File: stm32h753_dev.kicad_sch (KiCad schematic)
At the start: 88 parts, among them J1 Conn_02x38_Counter_Clockwise, J2 Conn_02x38_Counter_Clockwise, J3 USB_C_Receptacle_USB2.0_16P, J4 USB_C_Receptacle_USB2.0_16P, J5 DE9_Pins_MountingHoles, J6 Conn_01x05_Pin, J7 Conn_ARM_JTAG_SWD_10, SW1 SW_Push, SW2 SW_Push, U1 STM32H753IITx, U2 ST1S40IDR, U3 TPS2121RUX, U4 USB3300-EZK, U5 MCP2562-E-SN, U6 W25Q128JVS, Y1 SG-210STF, Y2 8MHz, Y3 Crystal

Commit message: pf13, pf14, pf15, pg0, add qspi to readme
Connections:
- net PF13: now reaches U1.63 (PF13)
- net PF13: now also J2.59 (Pin_59)
- net PF14: now reaches U1.64 (PF14)
- net PF14: now also J2.60 (Pin_60)
- net PF15: now reaches U1.65 (PF15)
- net PF15: now also J2.57 (Pin_57)
- net PG0: now reaches U1.66 (PG0)
- net PG0: now also J2.58 (Pin_58)
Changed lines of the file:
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@@
 	(wire
 		(pts
+			(xy 191.77 139.7) (xy 191.77 127)
+		)
+		(stroke
+			(width 0)
+			(type default)
+		)
+	)
+	(wire
+		(pts
 			(xy 189.23 44.45) (xy 189.23 55.88)
 		)
@@
 	(wire
 		(pts
+			(xy 270.51 139.7) (xy 270.51 127)
+		)
+		(stroke
+			(width 0)
+			(type default)
+		)
+	)
+	(wire
+		(pts
 			(xy 401.32 81.28) (xy 388.62 81.28)
 		)
@@
 	(wire
 		(pts
+			(xy 323.85 114.3) (xy 336.55 114.3)
+		)
+		(stroke
+			(width 0)
+			(type default)
+		)
+	)
+	(wire
+		(pts
 			(xy 401.32 48.26) (xy 388.62 48.26)
 		)
@@
 	(wire
 		(pts
+			(xy 267.97 139.7) (xy 267.97 127)
+		)
+		(stroke
+			(width 0)
+			(type default)
+		)
+	)
+	(wire
+		(pts
 			(xy 85.09 86.36) (xy 85.09 88.9)
 		)
@@
 	(wire
 		(pts
+			(xy 323.85 111.76) (xy 336.55 111.76)
+		)
+		(stroke
+			(width 0)
+			(type default)
+		)
+	)
+	(wire
+		(pts
 			(xy 229.87 266.7) (xy 248.92 266.7)
 		)
@@
 	(wire
 		(pts
+			(xy 361.95 111.76) (xy 349.25 111.76)
+		)
+		(stroke
+			(width 0)
+			(type default)
+		)
+	)
+	(wire
+		(pts
 			(xy 66.04 265.43) (xy 68.58 265.43)
 		)
@@
 	(wire
 		(pts
+			(xy 361.95 114.3) (xy 349.25 114.3)
+		)
+		(stroke
+			(width 0)
+			(type default)
+		)
+	)
+	(wire
+		(pts
 			(xy 151.13 139.7) (xy 151.13 127)
 		)
@@
 	(wire
 		(pts
+			(xy 273.05 127) (xy 273.05 132.08)
+		)
+		(stroke
+			(width 0)
+			(type default)
+		)
+	)
+	(wire
+		(pts
 			(xy 113.03 44.45) (xy 113.03 55.88)
 		)
@@
 		)
 	)
+	(label "PF14"
+		(at 361.95 114.3 180)
+		(effects
+			(font
+				(size 1.27 1.27)
+			)
+			(justify right bottom)
+		)
+	)
 	(label "PG14"
 		(at 227.33 139.7 90)
@@
 		)
 	)
+	(label "PG0"
+		(at 361.95 111.76 180)
+		(effects
+			(font
+				(size 1.27 1.27)
+			)
+			(justify right bottom)
+		)
+	)
 	(label "PF5"
 		(at 363.22 104.14 0)
@@
 		)
 	)
+	(label "PF15"
+		(at 273.05 132.08 90)
+		(effects
+			(font
+				(size 1.27 1.27)
+			)
+			(justify left bottom)
+		)
+	)
 	(label "PG12"
 		(at 363.22 68.58 0)
@@
 		)
 	)
+	(label "PF15"
+		(at 323.85 111.76 0)
+		(effects
+			(font
+				(size 1.27 1.27)
+			)
+			(justify left bottom)
+		)
+	)
 	(label "PB7"
 		(at 401.32 76.2 180)
@@
 		)
 	)
+	(label "PF13"
+		(at 323.85 114.3 0)
+		(effects
+			(font
+				(size 1.27 1.27)
+			)
+			(justify left bottom)
+		)
+	)
 	(label "CAN_RX"
 		(at 363.22 129.54 0)
@@
 		)
 	)
+	(label "PF13"
+		(at 267.97 139.7 90)
+		(effects
+			(font
+				(size 1.27 1.27)
+			)
+			(justify left bottom)
+		)
+	)
 	(label "ULPI_NXT"
 		(at 233.68 241.3 0)
@@
 		)
 	)
+	(label "PF14"
+		(at 270.51 139.7 90)
+		(effects
+			(font
+				(size 1.27 1.27)
+			)
+			(justify left bottom)
+		)
+	)
 	(label "PA7"
 		(at 113.03 44.45 270)
@@
 		(effects
 			(font
+				(size 1.27 1.27)
+			)
+			(justify left bottom)
+		)
+	)
+	(label "PG0"
+		(at 191.77 139.7 90)
+		(effects
+			(font

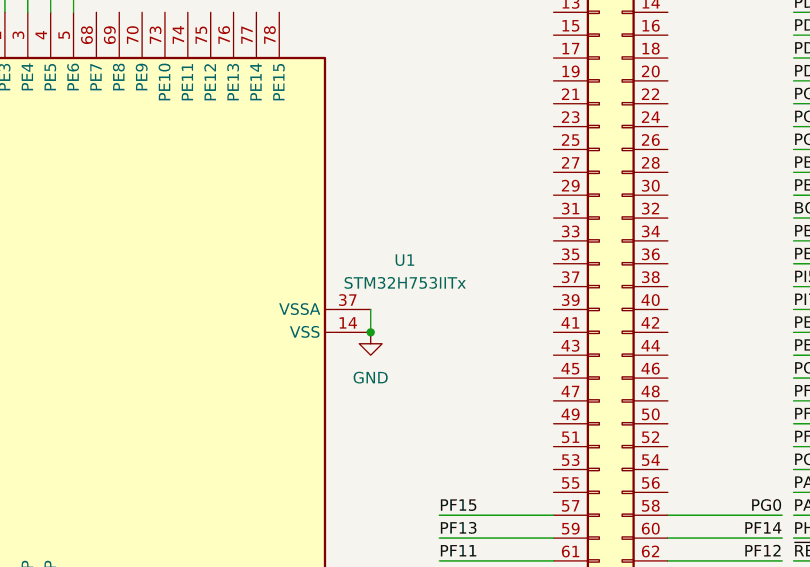
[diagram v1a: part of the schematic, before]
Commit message: change all references from 753 to 743
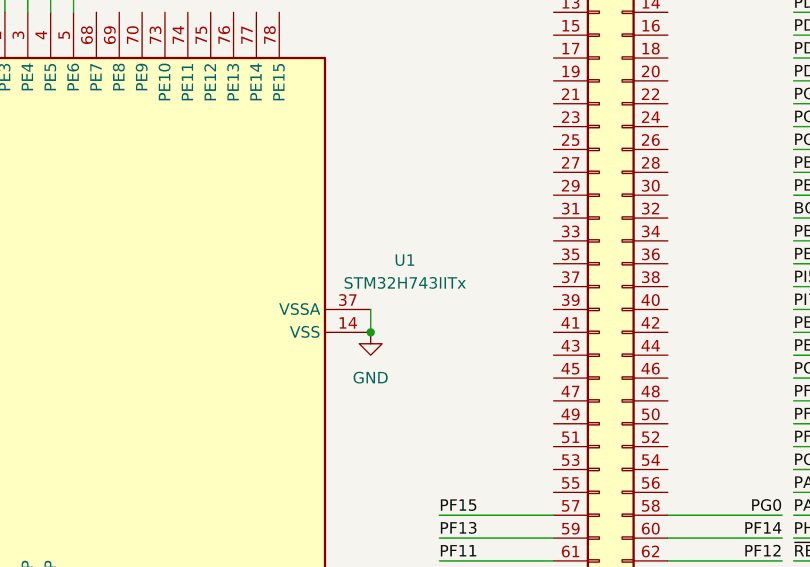
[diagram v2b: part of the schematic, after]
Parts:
- U1: value STM32H753IITx -> STM32H743IITx; symbol MCU_ST_STM32H7:STM32H753IITx -> MCU_ST_STM32H7:STM32H743IITx
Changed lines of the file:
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@@
 	)
 	(symbol
-		(lib_id "MCU_ST_STM32H7:STM32H753IITx")
+		(lib_id "MCU_ST_STM32H7:STM32H743IITx")
 		(at 201.93 91.44 90)
 		(unit 1)
@@
 			)
 		)
-		(property "Value" "STM32H753IITx"
+		(property "Value" "STM32H743IITx"
 			(at 320.04 85.9946 90)
 			(show_name no)
@@
 			)
 		)
-		(property "Datasheet" "https://www.st.com/resource/en/datasheet/stm32h753ii.pdf"
+		(property "Datasheet" "https://www.st.com/resource/en/datasheet/stm32h743ii.pdf"
 			(at 201.93 91.44 0)
 			(hide yes)

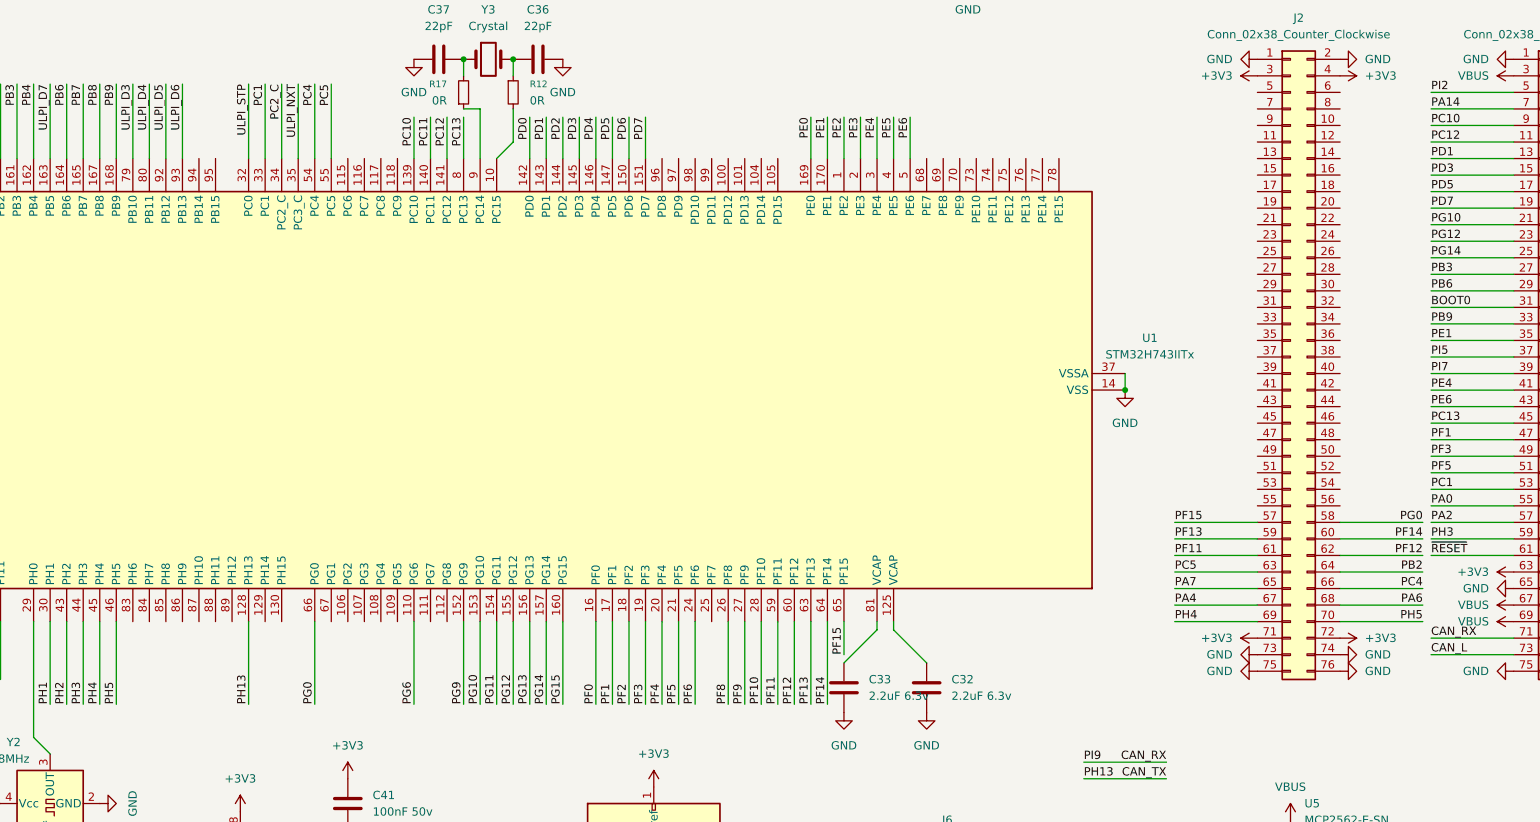
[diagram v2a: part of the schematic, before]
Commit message: more io routing, pinion experimentation
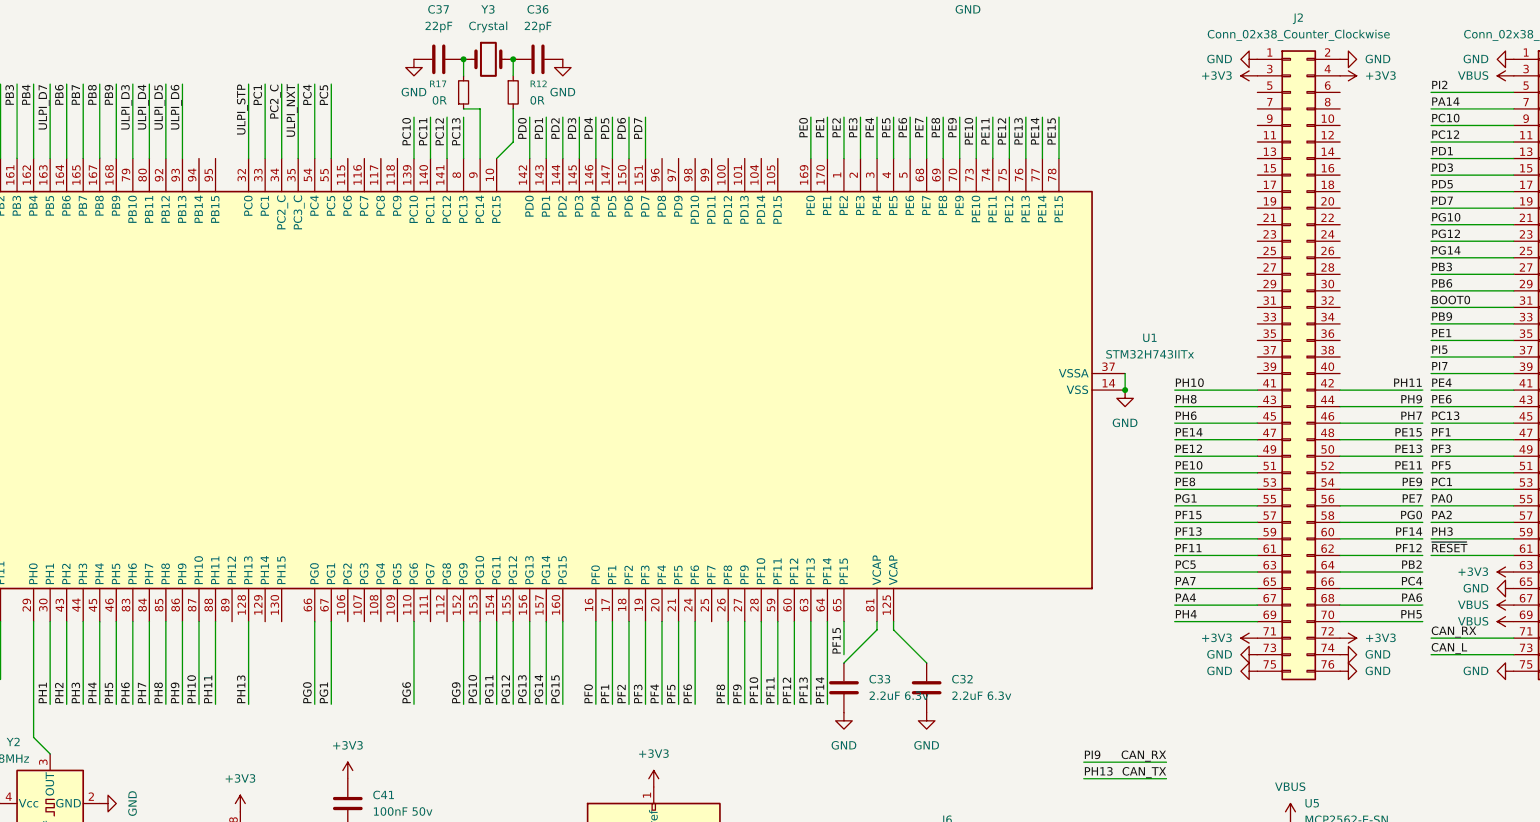
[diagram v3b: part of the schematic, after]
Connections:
- net PG1: now reaches U1.67 (PG1)
- net PG1: now also J2.55 (Pin_55)
- net PE7: now reaches U1.68 (PE7)
- net PE7: now also J2.56 (Pin_56)
- net PE8: now reaches U1.69 (PE8)
- net PE8: now also J2.53 (Pin_53)
- net PE9: now reaches U1.70 (PE9)
- net PE9: now also J2.54 (Pin_54)
- net PE10: now reaches U1.73 (PE10)
- net PE10: now also J2.51 (Pin_51)
- net PE11: now reaches U1.74 (PE11)
- net PE11: now also J2.52 (Pin_52)
- net PE12: now reaches U1.75 (PE12)
- net PE12: now also J2.49 (Pin_49)
- net PE13: now reaches U1.76 (PE13)
- net PE13: now also J2.50 (Pin_50)
- net PE14: now reaches U1.77 (PE14)
- net PE14: now also J2.47 (Pin_47)
- net PE15: now reaches U1.78 (PE15)
- net PE15: now also J2.48 (Pin_48)
- net PH6: now reaches U1.83 (PH6)
- net PH6: now also J2.45 (Pin_45)
- net PH7: now reaches U1.84 (PH7)
- net PH7: now also J2.46 (Pin_46)
- net PH8: now reaches U1.85 (PH8)
- net PH8: now also J2.43 (Pin_43)
- net PH9: now reaches U1.86 (PH9)
- net PH9: now also J2.44 (Pin_44)
- net PH10: now reaches U1.87 (PH10)
- net PH10: now also J2.41 (Pin_41)
- net PH11: now reaches U1.88 (PH11)
- net PH11: now also J2.42 (Pin_42)

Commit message: rgb led, route io
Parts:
- added D3: LED_RGB, LED_SMD:LED_RGB_Wuerth-PLCC4_3.2x2.8mm_150141M173100, symbol Device:LED_ARGB
- added Q1, Q2, Q3: BSS138, Package_TO_SOT_SMD:SOT-323_SC-70, symbol Transistor_FET:BSS138
- added R21, R22: 5.1R, Resistor_SMD:R_0402_1005Metric, symbol Device:R
- added R23: 68R, Resistor_SMD:R_0402_1005Metric, symbol Device:R
- added R24, R25, R26: 1k, Resistor_SMD:R_0402_1005Metric, symbol Device:R
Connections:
- net +3V3: now also J2.5 (Pin_5), J2.6 (Pin_6), D3.1 (A)
- net GND: now also J1.60 (Pin_60), J1.62 (Pin_62), J1.64 (Pin_64), J2.10 (Pin_10), J2.11 (Pin_11), J2.12 (Pin_12), J2.7 (Pin_7), J2.8 (Pin_8), J2.9 (Pin_9), Q1.2 (S), Q2.2 (S), Q3.2 (S)
- net PI0: now also J2.13 (Pin_13)
- net PI1: now also J2.14 (Pin_14)
- net PD12: now reaches U1.100 (PD12)
- net PD12: now also J2.34 (Pin_34)
- net PD13: now reaches U1.101 (PD13)
- net PD13: now also J2.31 (Pin_31)
- net PD14: now reaches U1.104 (PD14)
- net PD14: now also J2.32 (Pin_32)
- net PD15: now reaches U1.105 (PD15)
- net PD15: now also J2.29 (Pin_29)
- net PG2: now reaches U1.106 (PG2)
- net PG2: now also J2.30 (Pin_30)
- net PG3: now reaches U1.107 (PG3)
- net PG3: now also J2.27 (Pin_27)
- net PG4: now reaches U1.108 (PG4)
- net PG4: now also J2.28 (Pin_28)
- net PG5: now reaches U1.109 (PG5)
- net PG5: now also J2.25 (Pin_25)
- net PG7: now reaches U1.111 (PG7)
- net PG7: now also J2.26 (Pin_26)
- net PG8: now reaches U1.112 (PG8)
- net PG8: now also J2.23 (Pin_23)
- net PC6: now reaches U1.115 (PC6)
- net PC6: now also J2.24 (Pin_24)
- net PC7: now reaches U1.116 (PC7)
- net PC7: now also J2.21 (Pin_21)
- net PC8: now reaches U1.117 (PC8)
- net PC8: now also J2.22 (Pin_22)
- net PC9: now reaches U1.118 (PC9)
- net PC9: now also J2.20 (Pin_20)
- net PA8: now reaches U1.119 (PA8)
- net PA8: now also J2.19 (Pin_19)
- net PA9: now reaches U1.120 (PA9)
- net PA9: now also J2.17 (Pin_17)
- net PA10: now reaches U1.121 (PA10)
- net PA10: now also J2.18 (Pin_18)
- net PH14: now reaches U1.129 (PH14)
- net PH14: now also J2.15 (Pin_15)
- net PH15: now reaches U1.130 (PH15)
- net PH15: now also J2.16 (Pin_16)
- net PH12: now reaches U1.89 (PH12)
- net PH12: now also J2.39 (Pin_39)
- net PB14: now reaches U1.94 (PB14)
- net PB14: now also J2.40 (Pin_40)
- net PB15: now reaches U1.95 (PB15)
- net PB15: now also J2.37 (Pin_37)
- net PD8: now reaches U1.96 (PD8)
- net PD8: now also J2.38 (Pin_38)
- net PD9: now reaches U1.97 (PD9)
- net PD9: now also J2.35 (Pin_35)
- net PD10: now reaches U1.98 (PD10)
- net PD10: now also J2.36 (Pin_36)
- net PD11: now reaches U1.99 (PD11)
- net PD11: now also J2.33 (Pin_33)
- new net: Q2.1 (G), R25.2
- new net: Q2.3 (D), R21.1
- new net: Q3.1 (G), R26.2
- new net: Q3.3 (D), R23.1
- new net: Q1.3 (D), R22.1
- new net: D3.4 (BK), R22.2
- new net: Q1.1 (G), R24.2
- new net: D3.3 (GK), R21.2
- new net: D3.2 (RK), R23.2

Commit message: rgb gates, pinion changes
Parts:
- J5: value DE9_Pins_MountingHoles -> DE9_Pins_MH
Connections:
- net PA6: now also R26.1
- net PA7: now also R25.1
- net PC8: now also R24.1
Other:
- moved on the sheet: C1, C10, C11, C12, C13, C14, C2, C3, C31, C32, C33, C34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

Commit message: power led
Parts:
- added D4: LED, LED_SMD:LED_0603_1608Metric, symbol Device:LED
- added R27: 300R, Resistor_SMD:R_0402_1005Metric, symbol Device:R
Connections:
- net GND: now also D4.1 (K)
- net VBUS: now also R27.2
- new net: D4.2 (A), R27.1
